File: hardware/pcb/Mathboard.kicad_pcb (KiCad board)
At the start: 2 copper layers, 95.6 x 74.3 mm, 44 parts, among them J1 TSW-112-06-T-S, J2 TSW-112-06-T-S, J4 Conn_01x07_Pin, SW1 SW_Push, SW10 SW_Push, SW11 SW_Push, SW12 SW_Push, SW13 SW_Push, SW14 SW_Push, SW15 SW_Push, SW16 SW_Push, SW17 PCM13SMTR, SW2 SW_Push, SW3 SW_Push, SW4 SW_Push, SW5 SW_Push, SW6 SW_Push, SW7 SW_Push, SW8 SW_Push, SW9 SW_Push

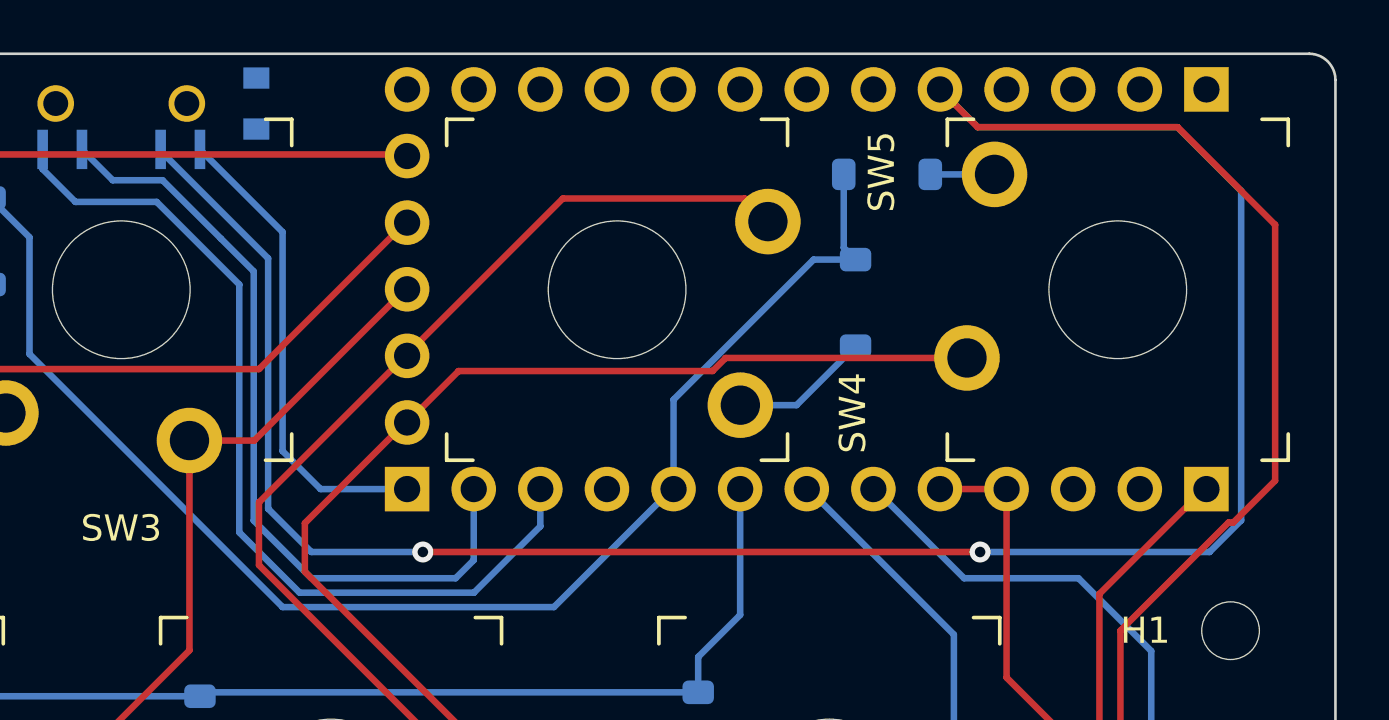
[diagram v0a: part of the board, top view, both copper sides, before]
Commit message: Bugfix: Set unicode mode switch pole to GND instead of VDD
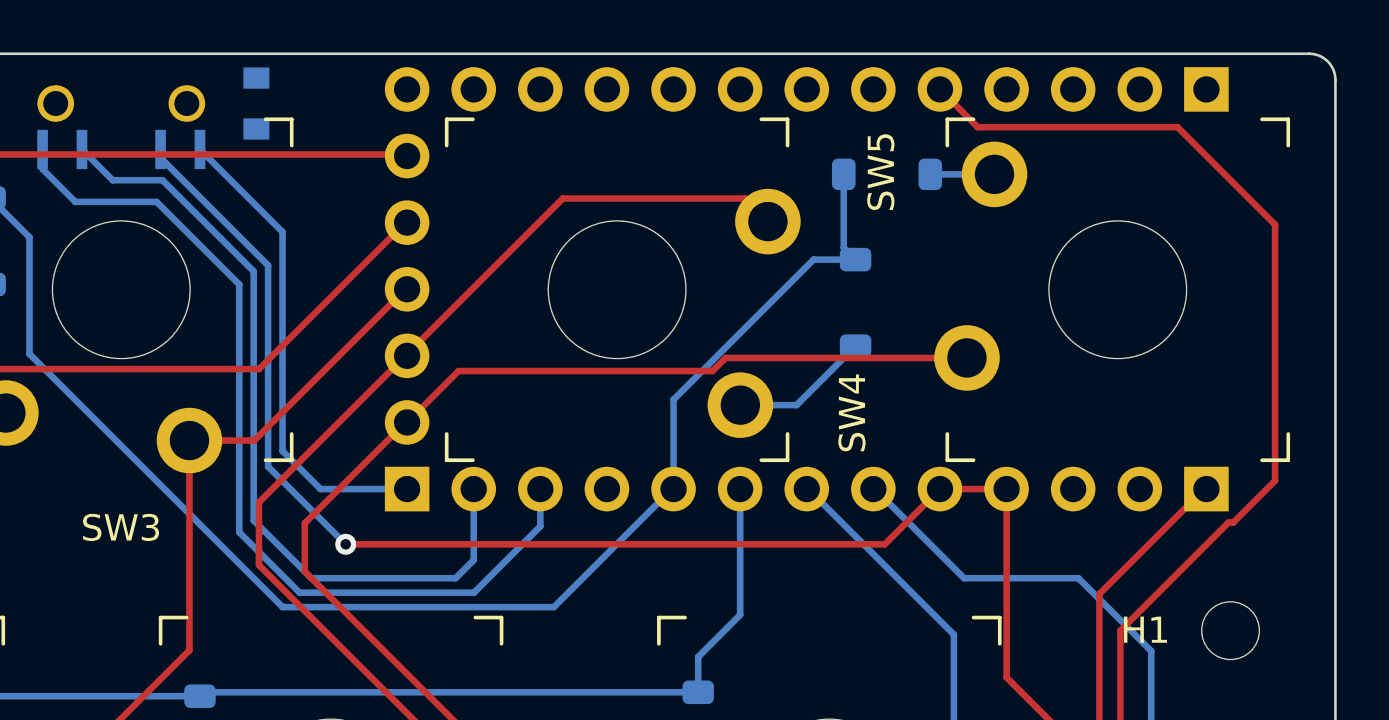
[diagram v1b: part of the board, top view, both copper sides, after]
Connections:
- SW17 pad 3: VDD -> GND
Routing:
- net VDD: track 239.3 -> 159.8 mm, vias 3 -> 1
- net GND: track 138.4 -> 180.0 mm, vias 1 -> 2
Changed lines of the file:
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@@
       (net 37 "Net-(J2-Pin_12)") (pinfunction "2") (pintype "passive"))
     (pad "3" smd rect (at 4.500002 0) (size 0.4064 1.499997) (layers "B.Cu" "B.Paste" "B.Mask")
-      (net 28 "VDD") (pinfunction "3") (pintype "passive"))
+      (net 30 "GND") (pinfunction "3") (pintype "passive"))
     (pad "4" smd rect (at 6.000001 0) (size 0.4064 1.499997) (layers "B.Cu" "B.Paste" "B.Mask")
       (net 38 "Net-(J4-Pin_1)") (pinfunction "4") (pintype "passive"))
@@
   (segment (start 105.15 98.85) (end 175.505635 98.85) (width 0.25) (layer "F.Cu") (net 28))
   (segment (start 94.75 109.25) (end 94.75 109.65) (width 0.25) (layer "F.Cu") (net 28))
-  (segment (start 166.05 61) (end 144.8 61) (width 0.25) (layer "F.Cu") (net 28))
   (segment (start 95.4 108.6) (end 105.15 98.85) (width 0.25) (layer "F.Cu") (net 28))
   (segment (start 95.4 108.6) (end 94.75 109.25) (width 0.25) (layer "F.Cu") (net 28))
-  (via (at 144.8 61) (size 0.8) (drill 0.4) (layers "F.Cu" "B.Cu") (net 28))
   (via (at 95.4 108.6) (size 0.8) (drill 0.4) (layers "F.Cu" "B.Cu") (net 28))
-  (via (at 166.05 61) (size 0.8) (drill 0.4) (layers "F.Cu" "B.Cu") (net 28))
-  (segment (start 138.9 59.35) (end 138.9 49.802241) (width 0.25) (layer "B.Cu") (net 28))
-  (segment (start 174.8 61) (end 166.05 61) (width 0.25) (layer "B.Cu") (net 28))
-  (segment (start 165.96 44.8) (end 173.58 44.8) (width 0.25) (layer "B.Cu") (net 28))
-  (segment (start 176.005 47.225) (end 176.005 59.795) (width 0.25) (layer "B.Cu") (net 28))
-  (segment (start 173.58 44.8) (end 176.005 47.225) (width 0.25) (layer "B.Cu") (net 28))
-  (segment (start 144.8 61) (end 140.55 61) (width 0.25) (layer "B.Cu") (net 28))
-  (segment (start 140.55 61) (end 138.9 59.35) (width 0.25) (layer "B.Cu") (net 28))
-  (segment (start 134.800001 45.702242) (end 134.800001 45.648) (width 0.25) (layer "B.Cu") (net 28))
   (segment (start 93.075 108) (end 94.8 108) (width 0.25) (layer "B.Cu") (net 28))
   (segment (start 94.8 108) (end 95.4 108.6) (width 0.25) (layer "B.Cu") (net 28))
-  (segment (start 176.005 59.795) (end 174.8 61) (width 0.25) (layer "B.Cu") (net 28))
-  (segment (start 134.800001 45.250001) (end 134.800001 45.148) (width 0.25) (layer "B.Cu") (net 28))
-  (segment (start 164.52 43.36) (end 165.96 44.8) (width 0.25) (layer "B.Cu") (net 28))
-  (segment (start 138.9 49.802241) (end 134.800001 45.702242) (width 0.25) (layer "B.Cu") (net 28))
+  (segment (start 164.52 58.6) (end 162.414 60.706) (width 0.25) (layer "F.Cu") (net 30))
   (segment (start 175.05 97.75) (end 98.45 97.75) (width 0.25) (layer "F.Cu") (net 30))
   (segment (start 167.06 65.787818) (end 177.15 75.877818) (width 0.25) (layer "F.Cu") (net 30))
@@
   (segment (start 177.15 75.877818) (end 177.15 95.65) (width 0.25) (layer "F.Cu") (net 30))
   (segment (start 167.06 58.6) (end 167.06 65.787818) (width 0.25) (layer "F.Cu") (net 30))
+  (segment (start 162.414 60.706) (end 141.859 60.706) (width 0.25) (layer "F.Cu") (net 30))
   (segment (start 177.15 95.65) (end 175.05 97.75) (width 0.25) (layer "F.Cu") (net 30))
   (via (at 90.85 105.35) (size 0.8) (drill 0.4) (layers "F.Cu" "B.Cu") (net 30))
+  (via (at 141.859 60.706) (size 0.8) (drill 0.4) (layers "F.Cu" "B.Cu") (net 30))
   (segment (start 91.525 106.025) (end 90.85 105.35) (width 0.25) (layer "B.Cu") (net 30))
+  (segment (start 141.859 60.706) (end 138.9 57.747) (width 0.25) (layer "B.Cu") (net 30))
+  (segment (start 138.9 57.747) (end 138.9 50.072182) (width 0.25) (layer "B.Cu") (net 30))
   (segment (start 91.525 108) (end 91.525 106.025) (width 0.25) (layer "B.Cu") (net 30))
+  (segment (start 134.800001 45.972183) (end 134.800001 45.648) (width 0.25) (layer "B.Cu") (net 30))
+  (segment (start 134.800001 45.250001) (end 134.800001 45.148) (width 0.25) (layer "B.Cu") (net 30))
+  (segment (start 138.9 50.072182) (end 134.800001 45.972183) (width 0.25) (layer "B.Cu") (net 30))
   (segment (start 173.98 59.22) (end 170.6 62.6) (width 0.25) (layer "F.Cu") (net 31))
   (segment (start 174 59.22) (end 173.98 59.22) (width 0.25) (layer "F.Cu") (net 31))

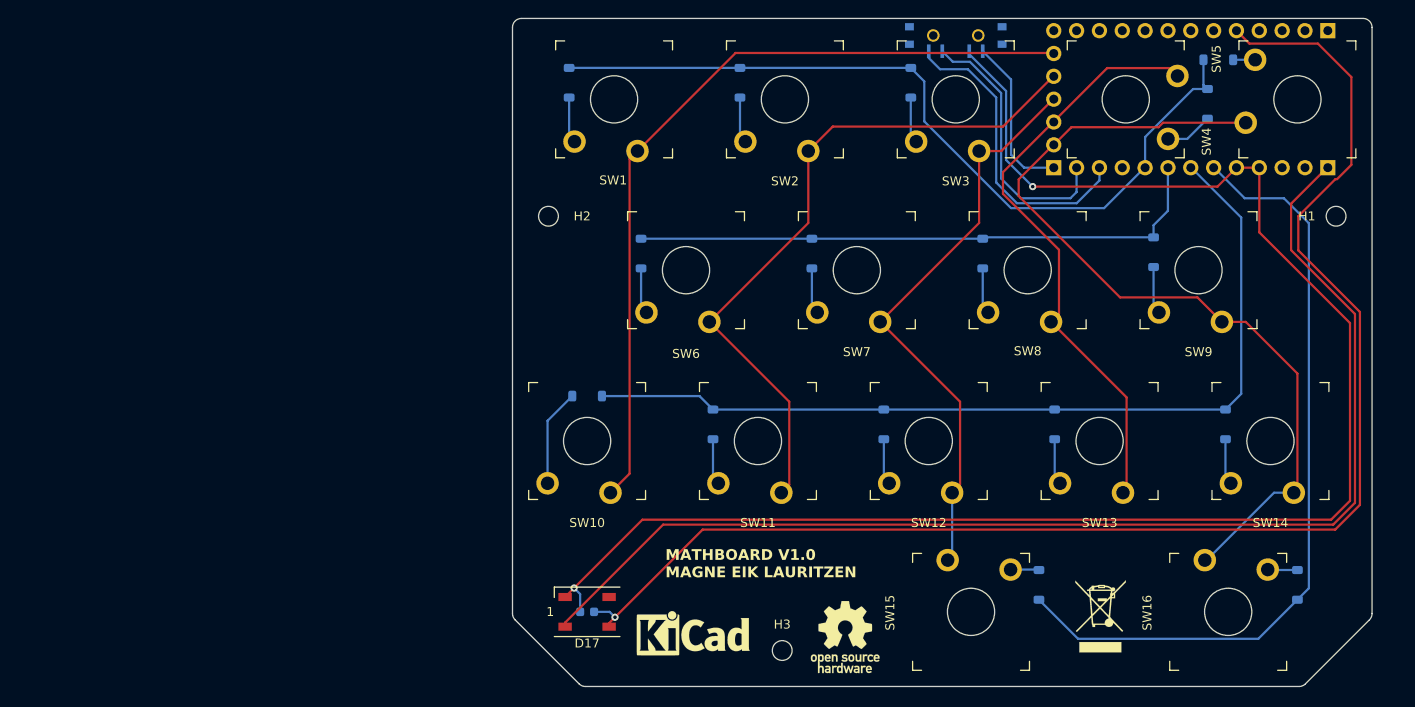
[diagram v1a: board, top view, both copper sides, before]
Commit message: Make assembly holes larger
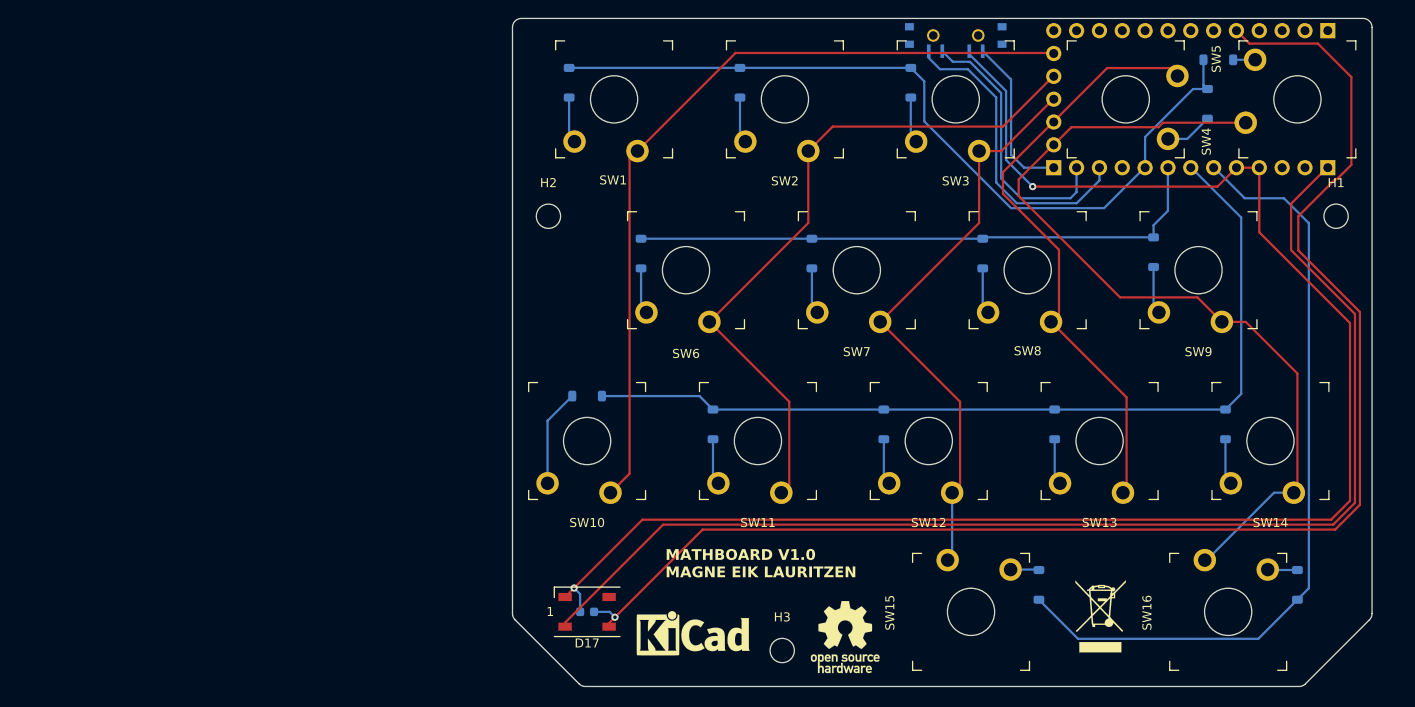
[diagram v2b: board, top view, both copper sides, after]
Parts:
- H1, H2, H3: footprint MountingHole:MountingHole_2.2mm_M2_DIN965 -> MountingHole:MountingHole_2.7mm
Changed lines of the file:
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@@
     )
   )
-  (footprint "MountingHole:MountingHole_2.2mm_M2_DIN965" (layer "F.Cu")
+  (footprint "MountingHole:MountingHole_2.7mm" (layer "F.Cu")
     (at 88 64)
-    (descr "Mounting Hole 2.2mm, no annular, M2, DIN965")
-    (tags "mounting hole 2.2mm no annular m2 din965")
+    (descr "Mounting Hole 2.7mm, no annular")
+    (tags "mounting hole 2.7mm no annular")
     (property "JLCPCB BOM" "0")
     (property "Sheetfile" "Mathboard.kicad_sch")
@@
     (property "ki_keywords" "mounting hole")
     (attr exclude_from_pos_files)
-    (fp_text reference "H2" (at 3.75 0) (layer "F.SilkS")
+    (fp_text reference "H2" (at 0 -3.7) (layer "F.SilkS")
         (effects (font (size 1 1) (thickness 0.15)))
     )
-    (fp_text value "MountingHole" (at 3.25 3.5) (layer "F.Fab")
+    (fp_text value "MountingHole" (at 0 3.7) (layer "F.Fab")
         (effects (font (size 1 1) (thickness 0.15)))
     )
-    (fp_text user "${REFERENCE}" (at 0 -2.75) (layer "F.Fab")
+    (fp_text user "${REFERENCE}" (at 0 0) (layer "F.Fab")
         (effects (font (size 1 1) (thickness 0.15)))
     )
-    (fp_circle (center 0 0) (end 1.9 0)
+    (fp_circle (center 0 0) (end 2.7 0)
       (stroke (width 0.15) (type solid)) (fill none) (layer "Cmts.User"))
-    (fp_circle (center 0 0) (end 2.15 0)
+    (fp_circle (center 0 0) (end 2.95 0)
       (stroke (width 0.05) (type solid)) (fill none) (layer "F.CrtYd"))
-    (pad "" np_thru_hole circle (at 0 0) (size 2.2 2.2) (drill 2.2) (layers "*.Cu" "*.Mask"))
+    (pad "" np_thru_hole circle (at 0 0) (size 2.7 2.7) (drill 2.7) (layers "*.Cu" "*.Mask"))
   )
-  (footprint "MountingHole:MountingHole_2.2mm_M2_DIN965" (layer "F.Cu")
+  (footprint "MountingHole:MountingHole_2.7mm" (layer "F.Cu")
     (at 175.6 64)
-    (descr "Mounting Hole 2.2mm, no annular, M2, DIN965")
-    (tags "mounting hole 2.2mm no annular m2 din965")
+    (descr "Mounting Hole 2.7mm, no annular")
+    (tags "mounting hole 2.7mm no annular")
     (property "JLCPCB BOM" "0")
     (property "Sheetfile" "Mathboard.kicad_sch")
@@
     (property "ki_keywords" "mounting hole")
     (attr exclude_from_pos_files)
-    (fp_text reference "H1" (at -3.25 0) (layer "F.SilkS")
+    (fp_text reference "H1" (at 0 -3.7) (layer "F.SilkS")
         (effects (font (size 1 1) (thickness 0.15)))
     )
-    (fp_text value "MountingHole" (at -3.5 3.25) (layer "F.Fab")
+    (fp_text value "MountingHole" (at 0 3.7) (layer "F.Fab")
         (effects (font (size 1 1) (thickness 0.15)))
     )
-    (fp_text user "${REFERENCE}" (at -3.25 0) (layer "F.Fab")
+    (fp_text user "${REFERENCE}" (at 0 0) (layer "F.Fab")
         (effects (font (size 1 1) (thickness 0.15)))
     )
-    (fp_circle (center 0 0) (end 1.9 0)
+    (fp_circle (center 0 0) (end 2.7 0)
       (stroke (width 0.15) (type solid)) (fill none) (layer "Cmts.User"))
-    (fp_circle (center 0 0) (end 2.15 0)
+    (fp_circle (center 0 0) (end 2.95 0)
       (stroke (width 0.05) (type solid)) (fill none) (layer "F.CrtYd"))
-    (pad "" np_thru_hole circle (at 0 0) (size 2.2 2.2) (drill 2.2) (layers "*.Cu" "*.Mask"))
+    (pad "" np_thru_hole circle (at 0 0) (size 2.7 2.7) (drill 2.7) (layers "*.Cu" "*.Mask"))
   )
   (footprint "Symbol:OSHW-Logo_7.5x8mm_SilkScreen" (layer "F.Cu")
@@
     )
   )
-  (footprint "MountingHole:MountingHole_2.2mm_M2_DIN965" (layer "F.Cu")
+  (footprint "MountingHole:MountingHole_2.7mm" (layer "F.Cu")
     (at 114 112.3)
-    (descr "Mounting Hole 2.2mm, no annular, M2, DIN965")
-    (tags "mounting hole 2.2mm no annular m2 din965")
+    (descr "Mounting Hole 2.7mm, no annular")
+    (tags "mounting hole 2.7mm no annular")
     (property "JLCPCB BOM" "0")
     (property "Sheetfile" "Mathboard.kicad_sch")
@@
     (property "ki_keywords" "mounting hole")
     (attr exclude_from_pos_files)
-    (fp_text reference "H3" (at 0 -2.9) (layer "F.SilkS")
+    (fp_text reference "H3" (at 0 -3.7) (layer "F.SilkS")
         (effects (font (size 1 1) (thickness 0.15)))
     )
-    (fp_text value "MountingHole" (at 0 -4.25) (layer "F.Fab")
+    (fp_text value "MountingHole" (at 0 3.7) (layer "F.Fab")
         (effects (font (size 1 1) (thickness 0.15)))
     )
@@
         (effects (font (size 1 1) (thickness 0.15)))
     )
-    (fp_circle (center 0 0) (end 1.9 0)
+    (fp_circle (center 0 0) (end 2.7 0)
       (stroke (width 0.15) (type solid)) (fill none) (layer "Cmts.User"))
-    (fp_circle (center 0 0) (end 2.15 0)
+    (fp_circle (center 0 0) (end 2.95 0)
       (stroke (width 0.05) (type solid)) (fill none) (layer "F.CrtYd"))
-    (pad "" np_thru_hole circle (at 0 0) (size 2.2 2.2) (drill 2.2) (layers "*.Cu" "*.Mask"))
+    (pad "" np_thru_hole circle (at 0 0) (size 2.7 2.7) (drill 2.7) (layers "*.Cu" "*.Mask"))
   )
   (footprint "Keyboard switches:SW_Gateron_LowProfile_THT" (layer "F.Cu")

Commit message: Update PCB and production files to revision 2
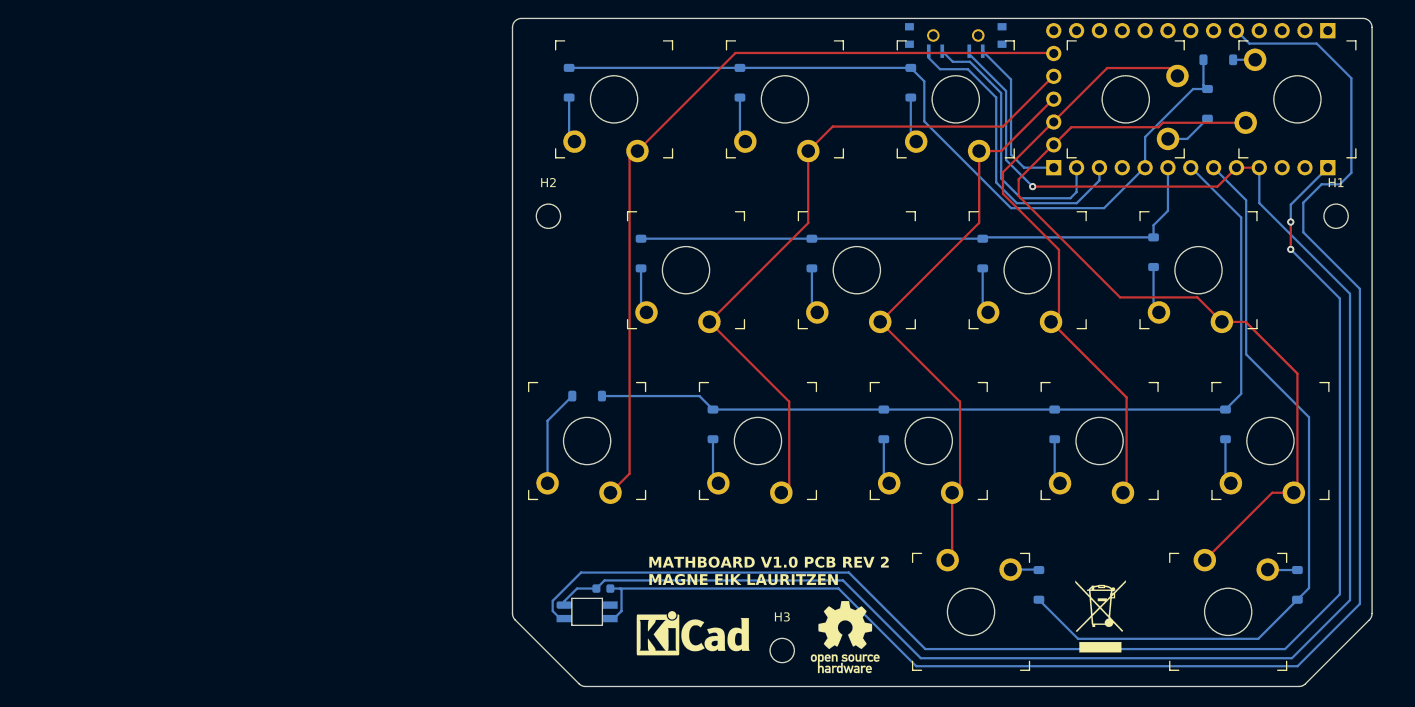
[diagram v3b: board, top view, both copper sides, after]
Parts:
- removed D17: WS2812B, LED_SMD:LED_WS2812B_PLCC4_5.0x5.0mm_P3.2mm
- added U2: ~, LED_SMD:SK6812-MINI-E, B.Cu at (92.3, 108.0)
- SW1, SW10, SW11, SW12, SW13, SW14, SW15, SW16, SW2, SW3, SW4, SW5, SW6, SW7, SW8, SW9: footprint Keyboard switches:SW_Gateron_LowProfile_THT -> key-switches:SW_Gateron_LowProfile_THT
- moved C1 3.16 mm to (94.1, 105.4)
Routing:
- net VDD: track 159.8 -> 173.4 mm, vias 1 -> 0
- net RGB_DIN: track 135.8 -> 149.1 mm, vias 0 -> 2
- net GND: track 180.0 -> 191.5 mm, vias 2 -> 1
- net ROW3: track 87.9 -> 85.3 mm
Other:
- board text added: "MATHBOARD V1.0 PCB REV 2 MAGNE EIK LAURITZEN"
- board text removed: "MATHBOARD V1.0 MAGNE EIK LAURITZEN"
